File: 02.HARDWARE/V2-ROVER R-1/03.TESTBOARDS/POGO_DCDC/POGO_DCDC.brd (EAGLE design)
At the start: 39 x 64 mm, 13 parts, among them J1 FEMALE 2x3

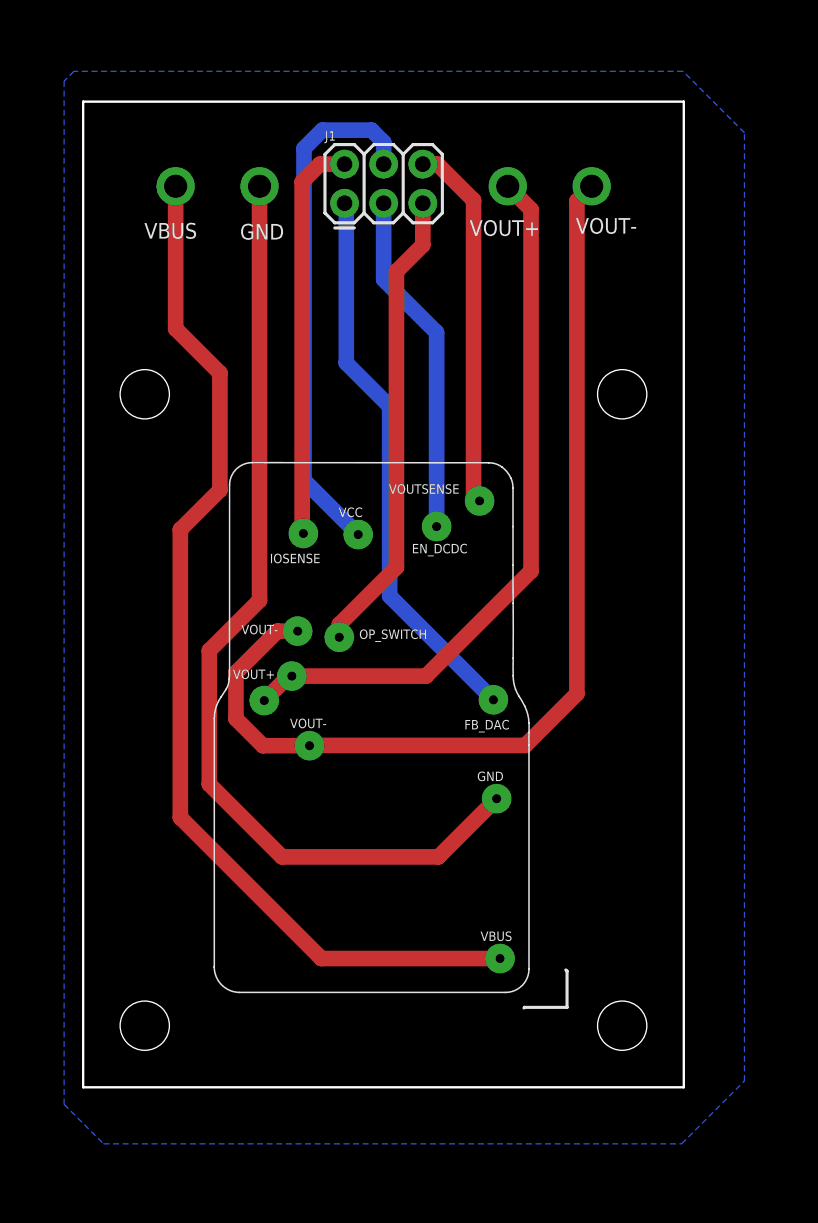
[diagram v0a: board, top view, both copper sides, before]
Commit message: Cierra el issue #38
Pin de VO+ desplazado
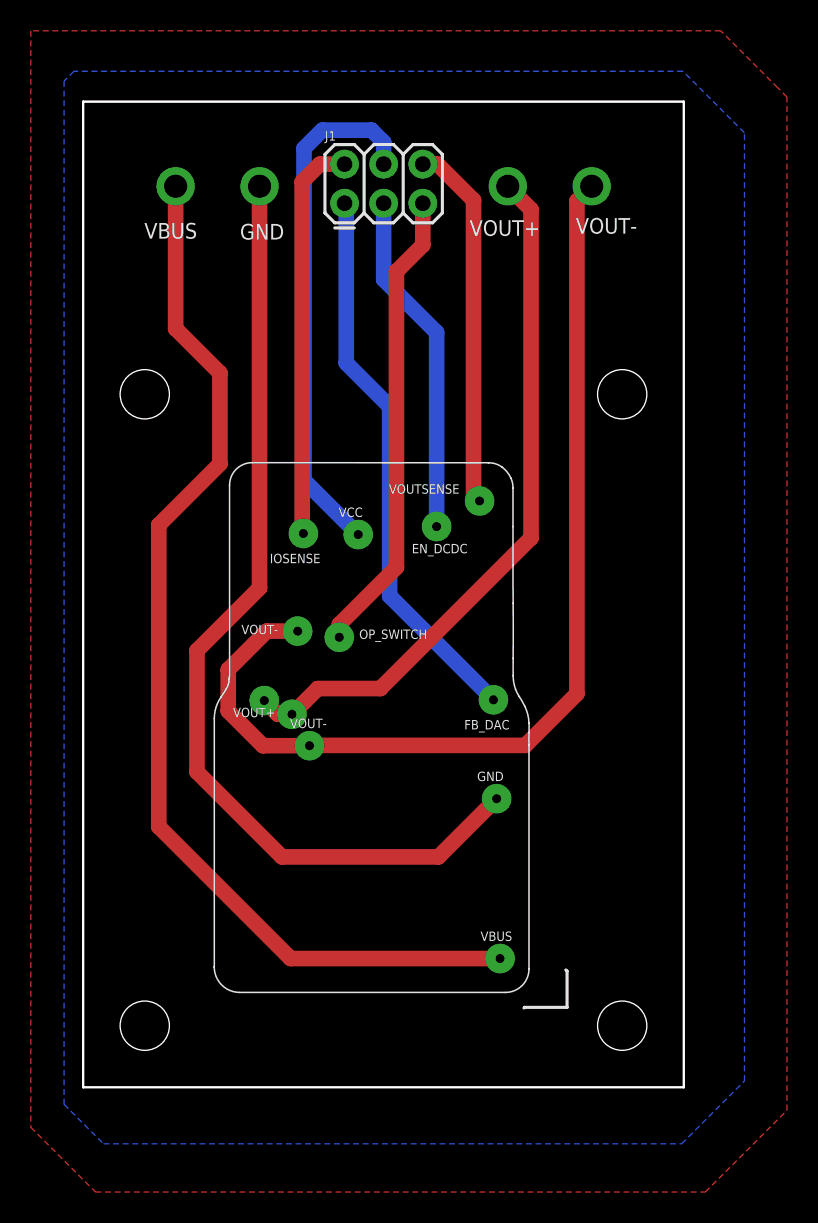
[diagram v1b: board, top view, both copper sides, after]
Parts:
- moved VOUT+ 2.48 mm to (62.6, 20.2)
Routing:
- net VBUS: track 67.8 -> 70.1 mm
- net VOUT-: track 65.7 -> 66.6 mm
- net GND: track 62.4 -> 63.0 mm
- net VOUT+: track 46.4 -> 45.9 mm
- added copper zone on layer 1, net GND
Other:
- board text added: "POGO_DCDC ROVER1K v2-Feb'23"
- board text removed: "POGO_DCDC ROVER1K v1-Ene'22"
